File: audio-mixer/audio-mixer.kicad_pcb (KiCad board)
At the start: 2 copper layers, 72.5 x 150 mm, 49 parts, among them J1 Input A1, J10 Pot, J11 Input B3, J12 Pot, J13 Pot, J14 Output A, J15 Pot, J16 Output B, J17 AudioJack4, J18 Power, J19 Power, J2 Pot, J3 Input A2, J4 Pot, J5 Input A3, J6 Pot, J7 Input B1, J8 Pot, J9 Input B2, SW1 Mono/Stereo, U1 TL072

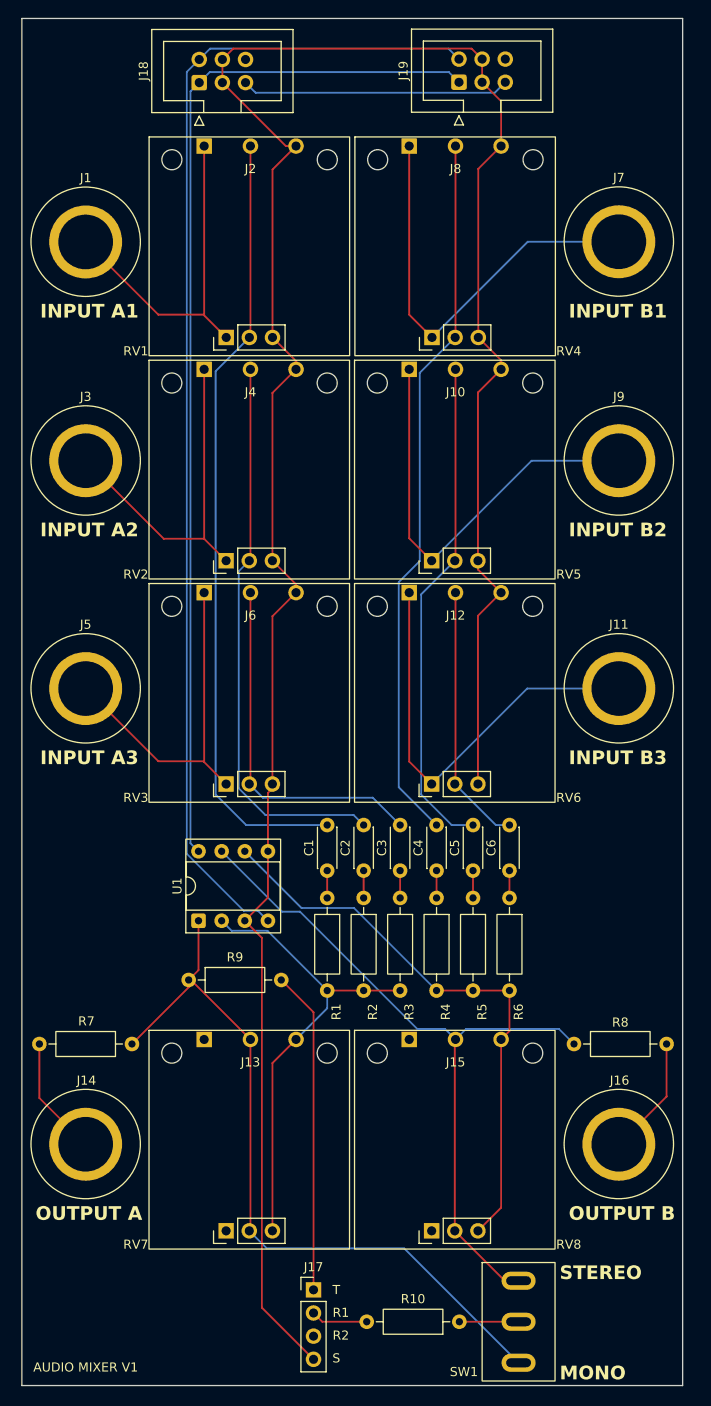
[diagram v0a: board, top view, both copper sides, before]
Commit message: More space for backup pot
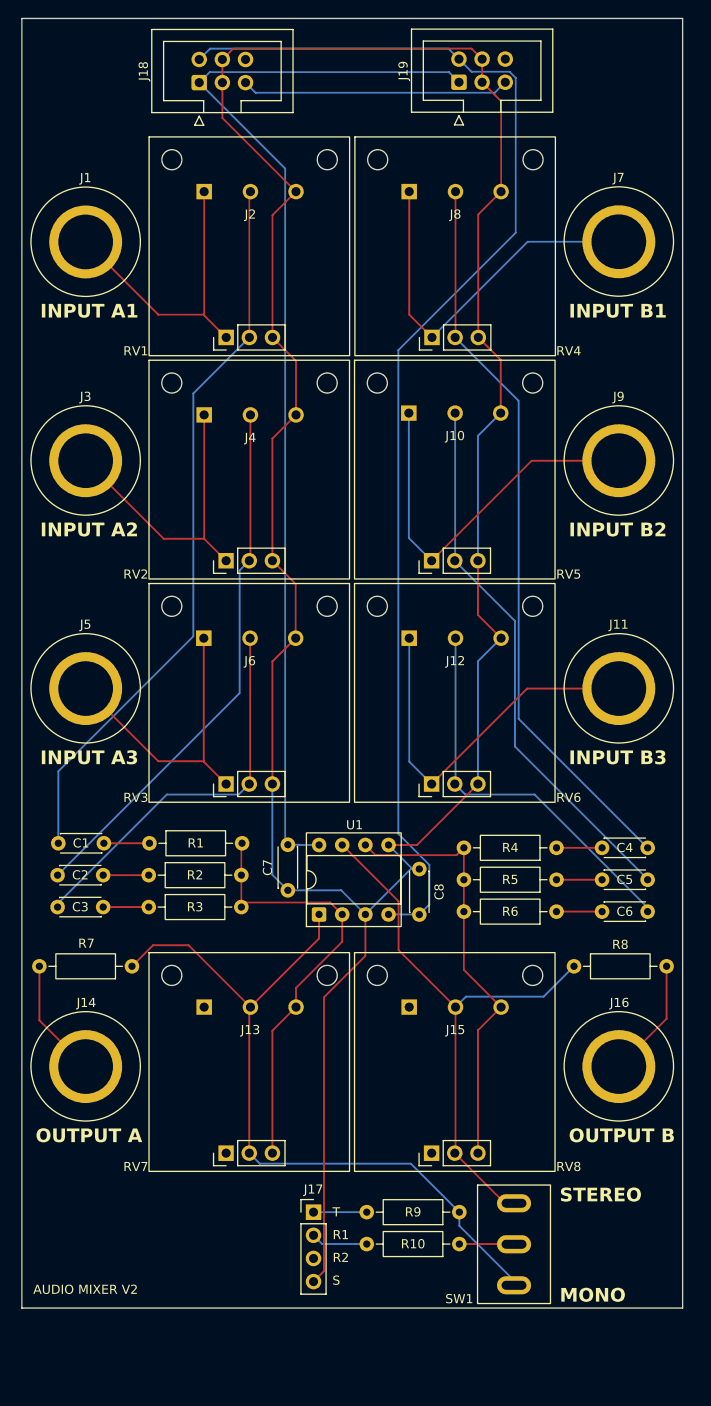
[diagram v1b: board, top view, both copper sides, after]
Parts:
- added C7: 100nF, Capacitor_THT:C_Disc_D4.3mm_W1.9mm_P5.00mm, F.Cu at (60.2, 118.2)
- added C8: 100nF, Capacitor_THT:C_Disc_D4.3mm_W1.9mm_P5.00mm, F.Cu at (74.6, 115.8)
- moved R9 39.1 mm to (79.0, 153.5), turned to 180 degrees
- moved C3 38.6 mm to (34.9, 120.0), turned to 0 degrees
- moved C2 34.0 mm to (34.9, 116.5), turned to 0 degrees
- moved C1 29.6 mm to (35.0, 113.0), turned to 0 degrees
- moved R3 27.6 mm to (44.9, 120.0), turned to 0 degrees
- moved R2 23.7 mm to (44.9, 116.5), turned to 0 degrees
- moved C4 23.3 mm to (99.7, 113.5), turned to 180 degrees
- moved R1 20.4 mm to (45.0, 113.0), turned to 0 degrees
- moved C5 20.1 mm to (99.7, 117.0), turned to 180 degrees
- moved C6 17.9 mm to (99.7, 120.5), turned to 180 degrees
- moved SW1 17.0 mm to (85.0, 157.0)
- moved R4 14.3 mm to (89.7, 113.5), turned to 180 degrees
- moved U1 13.2 mm to (63.6, 120.8)
- moved R5 9.38 mm to (89.7, 117.0), turned to 180 degrees
- moved F3 8.52 mm to (96.5, 156.5)
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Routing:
- net Net-(J17-PadT): track 35.5 -> 5.84 mm
- net GND: track 271.5 -> 292.9 mm
- net Net-(J15-Pin_2): track 78.7 -> 63.1 mm
- net Net-(J15-Pin_3): track 62.8 -> 47.8 mm
- net Net-(J12-Pin_2): track 28.9 -> 43.4 mm
- net -12V: track 129.1 -> 138.9 mm
- net Net-(J2-Pin_2): track 86.4 -> 80.2 mm
- net 12V: track 114.5 -> 120.5 mm
- net Net-(J7-Pin_1): track 46.9 -> 41.9 mm
- net Net-(J3-Pin_1): track 38.5 -> 33.5 mm
- net Net-(J11-Pin_1): track 46.9 -> 41.9 mm
- net Net-(J1-Pin_1): track 38.3 -> 33.3 mm
- net Net-(J5-Pin_1): track 38.3 -> 33.3 mm
- net Net-(J10-Pin_1): track 47.1 -> 42.3 mm
- net Net-(J10-Pin_2): track 55.3 -> 60.0 mm
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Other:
- board size 72.5 x 150 mm -> 72.5 x 141.5 mm
- board text added: "AUDIO MIXER V2"
- board text removed: "AUDIO MIXER V1"

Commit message: Various improvements
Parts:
- added G***: LOGO, modular2:ibis-small, F.Cu at (99.5, 159.0)

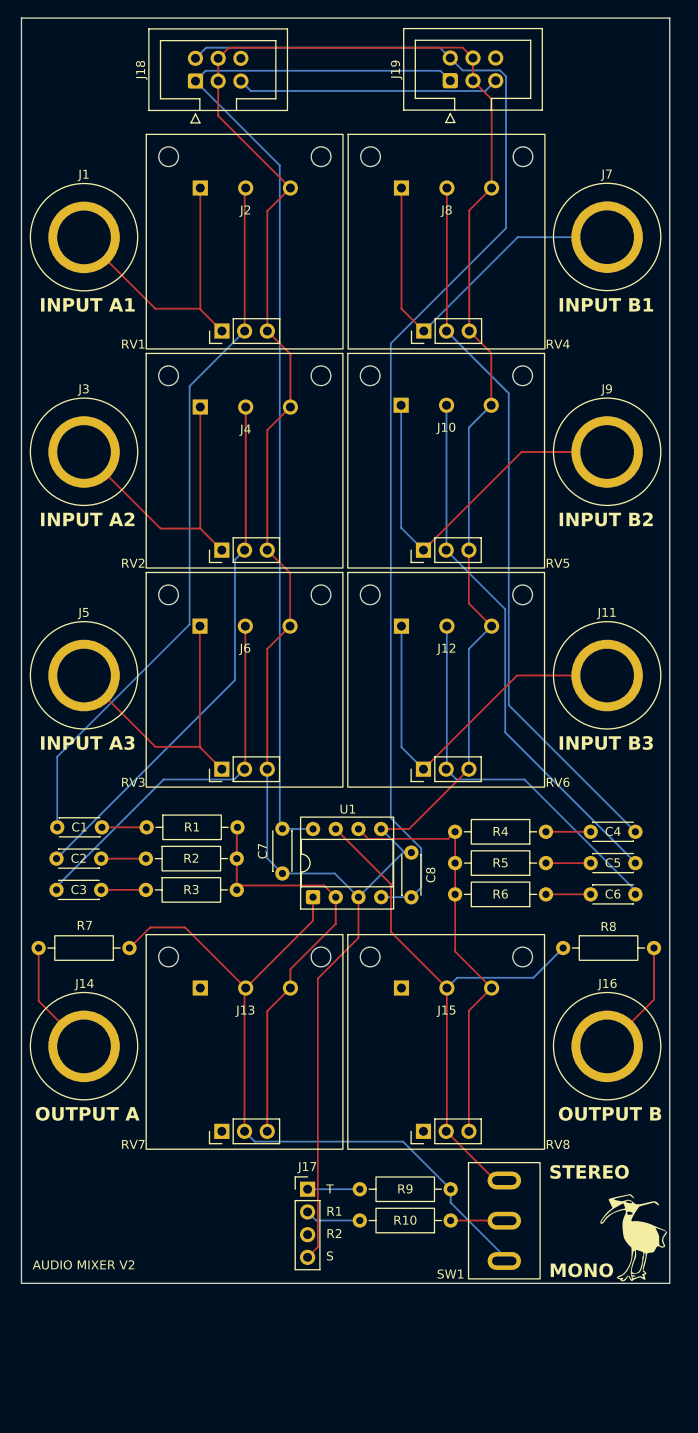
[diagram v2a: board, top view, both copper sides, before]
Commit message: Fix issues with audio mixer
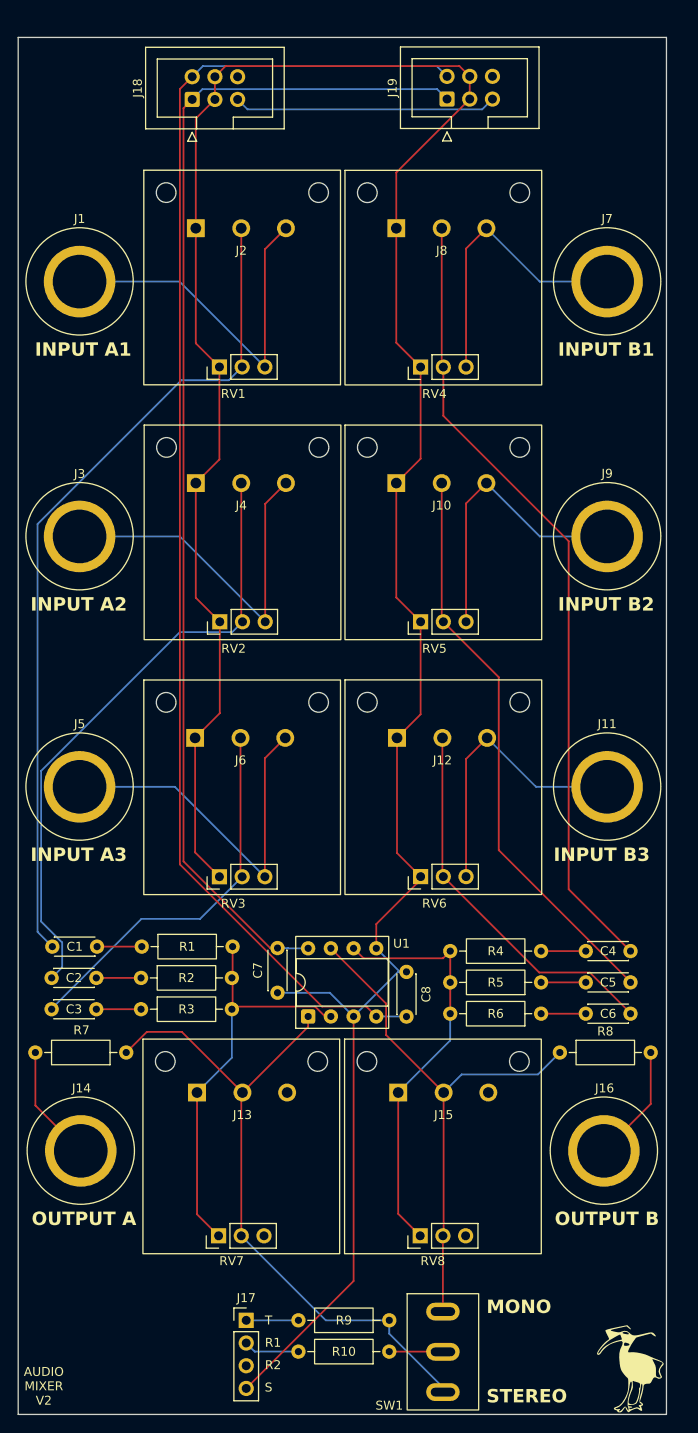
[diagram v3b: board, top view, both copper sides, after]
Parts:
- moved SW1 16.2 mm to (78.1, 171.7)
- moved J17 16.2 mm to (56.1, 168.1)
- moved R10 16.2 mm to (72.1, 171.6)
- moved R9 16.2 mm to (72.1, 168.1)
- moved G*** 14.7 mm to (99.1, 173.7)
- moved F3 14.7 mm to (96.1, 171.1)
- moved F4 14.7 mm to (37.6, 171.1)
- moved C8 13.4 mm to (74.1, 129.2)
- moved C1 13.4 mm to (34.5, 126.3)
- moved C4 13.4 mm to (99.1, 126.8)
- moved C7 13.4 mm to (59.6, 131.5)
- moved R1 13.4 mm to (44.5, 126.3)
- moved R4 13.4 mm to (89.1, 126.8)
- moved C2 13.4 mm to (34.4, 129.8)
- moved C3 13.4 mm to (34.4, 133.3)
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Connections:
- J10 pad 1: Net-(J10-Pin_1) -> GND
- J10 pad 3: GND -> Net-(J10-Pin_3)
- J12 pad 1: Net-(J11-Pin_1) -> GND
- J12 pad 3: GND -> Net-(J11-Pin_1)
- J13 pad 1: unconnected-(J13-Pin_1-Pad1) -> Net-(J13-Pin_1)
- J13 pad 3: Net-(J13-Pin_3) -> unconnected-(J13-Pin_3-Pad3)
- J15 pad 1: unconnected-(J15-Pin_1-Pad1) -> Net-(J15-Pin_1)
- J15 pad 3: Net-(J15-Pin_3) -> unconnected-(J15-Pin_3-Pad3)
- J2 pad 1: Net-(J1-Pin_1) -> GND
- J2 pad 3: GND -> Net-(J1-Pin_1)
- J4 pad 1: Net-(J3-Pin_1) -> GND
- J4 pad 3: GND -> Net-(J3-Pin_1)
- J6 pad 1: Net-(J5-Pin_1) -> GND
- J6 pad 3: GND -> Net-(J5-Pin_1)
- J8 pad 1: Net-(J7-Pin_1) -> GND
- J8 pad 3: GND -> Net-(J7-Pin_1)
- J9 pad 1: Net-(J10-Pin_1) -> Net-(J10-Pin_3)
- R1 pad 2: Net-(J13-Pin_3) -> Net-(J13-Pin_1)
- R2 pad 2: Net-(J13-Pin_3) -> Net-(J13-Pin_1)
- R3 pad 2: Net-(J13-Pin_3) -> Net-(J13-Pin_1)
- R4 pad 2: Net-(J15-Pin_3) -> Net-(J15-Pin_1)
- R5 pad 2: Net-(J15-Pin_3) -> Net-(J15-Pin_1)
- R6 pad 2: Net-(J15-Pin_3) -> Net-(J15-Pin_1)
- RV1 pad 1: Net-(J1-Pin_1) -> GND
- RV1 pad 3: GND -> Net-(J1-Pin_1)
- RV2 pad 1: Net-(J3-Pin_1) -> GND
- RV2 pad 3: GND -> Net-(J3-Pin_1)
- RV3 pad 1: Net-(J5-Pin_1) -> GND
- RV3 pad 3: GND -> Net-(J5-Pin_1)
- RV4 pad 1: Net-(J7-Pin_1) -> GND
- RV4 pad 3: GND -> Net-(J7-Pin_1)
- RV5 pad 1: Net-(J10-Pin_1) -> GND
- RV5 pad 3: GND -> Net-(J10-Pin_3)
- RV6 pad 1: Net-(J11-Pin_1) -> GND
- RV6 pad 3: GND -> Net-(J11-Pin_1)
- RV7 pad 1: unconnected-(RV7-Pad1) -> Net-(J13-Pin_1)
- RV7 pad 3: Net-(J13-Pin_3) -> unconnected-(RV7-Pad3)
- RV8 pad 1: unconnected-(RV8-Pad1) -> Net-(J15-Pin_1)
- RV8 pad 3: Net-(J15-Pin_3) -> unconnected-(RV8-Pad3)
- U1 pad 2: Net-(J13-Pin_3) -> Net-(J13-Pin_1)
- U1 pad 6: Net-(J15-Pin_3) -> Net-(J15-Pin_1)
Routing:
- net Net-(J13-Pin_3): track 48.2 -> 0.00 mm
- net Net-(J15-Pin_3): track 47.8 -> 0.00 mm
- net Net-(J15-Pin_1): track 0.00 -> 46.9 mm
- net Net-(J13-Pin_1): track 0.00 -> 46.6 mm
- net Net-(J10-Pin_1): track 42.3 -> 0.00 mm
- net Net-(J10-Pin_3): track 0.00 -> 32.4 mm
- net Net-(J2-Pin_2): track 80.2 -> 93.8 mm
- net 12V: track 120.5 -> 133.0 mm
- net -12V: track 138.9 -> 150.5 mm
- net Net-(J4-Pin_2): track 59.3 -> 69.6 mm
- net Net-(J11-Pin_1): track 41.9 -> 32.2 mm
- net GND: track 292.9 -> 302.6 mm
- net Net-(J7-Pin_1): track 41.9 -> 32.4 mm
- net Net-(J8-Pin_2): track 80.8 -> 89.6 mm
- net Net-(J5-Pin_1): track 33.3 -> 41.4 mm
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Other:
- board size 72.5 x 141.5 mm -> 72.5 x 154 mm

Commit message: Various fixes
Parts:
- added J20: Power, Connector_IDC:IDC-Header_2x03_P2.54mm_Vertical, F.Cu at (83.5, 31.5)
- moved J19 14.2 mm to (64.4, 31.6)
- moved J18 4.68 mm to (45.4, 31.5)
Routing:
- net GND: track 302.6 -> 324.8 mm
- net 5V: track 29.4 -> 40.0 mm
- net 12V: track 133.0 -> 139.2 mm
- net -12V: track 150.5 -> 152.8 mm

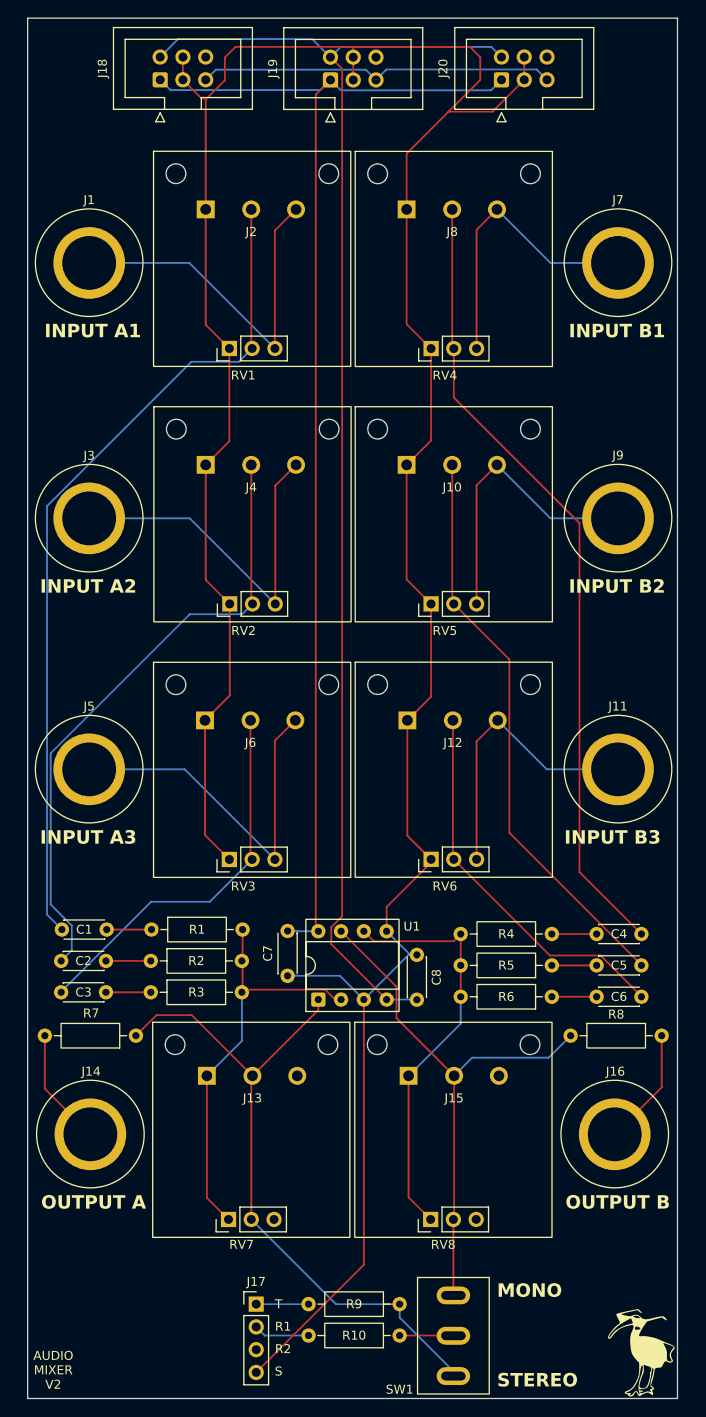
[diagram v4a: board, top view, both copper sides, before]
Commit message: Fix inverted output in audio mixer
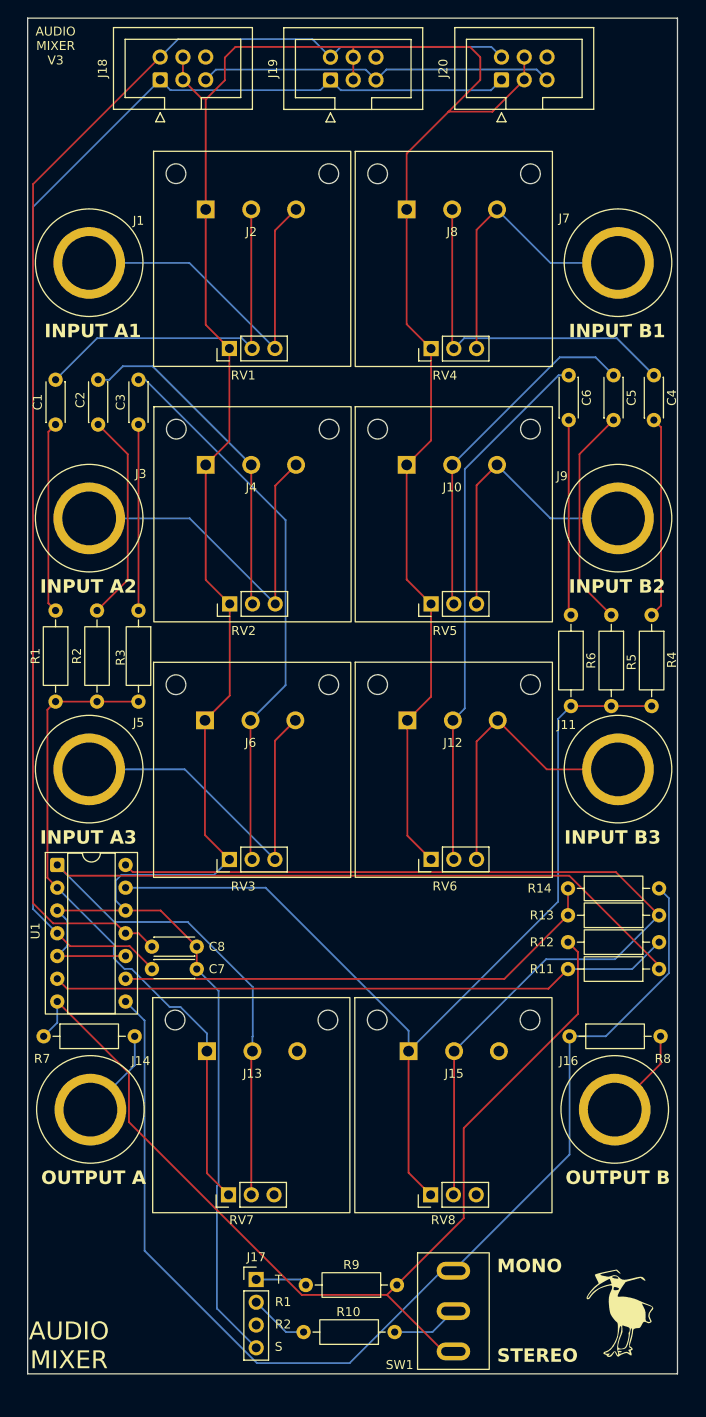
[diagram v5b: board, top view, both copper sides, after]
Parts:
- added R11: 100K, Resistor_THT:R_Axial_DIN0207_L6.3mm_D2.5mm_P10.16mm_Horizontal, F.Cu at (101.1, 130.8)
- added R12: 100K, Resistor_THT:R_Axial_DIN0207_L6.3mm_D2.5mm_P10.16mm_Horizontal, F.Cu at (101.1, 127.8)
- added R13: 100K, Resistor_THT:R_Axial_DIN0207_L6.3mm_D2.5mm_P10.16mm_Horizontal, F.Cu at (101.1, 124.8)
- added R14: 100K, Resistor_THT:R_Axial_DIN0207_L6.3mm_D2.5mm_P10.16mm_Horizontal, F.Cu at (90.9, 121.8)
- U1: value TL072 -> TL074; footprint Package_DIP:DIP-8_W7.62mm_Socket -> Package_DIP:DIP-14_W7.62mm_Socket
- moved C6 69.8 mm to (91.0, 64.5), turned to -90 degrees
- moved C3 68.9 mm to (43.0, 65.0), turned to -90 degrees
- moved C5 65.9 mm to (96.0, 64.5), turned to -90 degrees
- moved C2 65.0 mm to (38.5, 65.0), turned to -90 degrees
- moved C4 62.4 mm to (100.5, 64.5), turned to -90 degrees
- moved C1 61.3 mm to (33.8, 65.0), turned to -90 degrees
- moved R6 42.6 mm to (91.2, 91.2), turned to -90 degrees
- moved R3 42.6 mm to (43.0, 90.8), turned to -90 degrees
- moved R5 39.7 mm to (95.8, 91.2), turned to -90 degrees
- moved R2 39.5 mm to (38.4, 90.8), turned to -90 degrees
- moved R4 37.3 mm to (100.2, 91.2), turned to -90 degrees
- moved R1 37.2 mm to (33.8, 90.8), turned to -90 degrees
- moved U1 32.8 mm to (33.9, 119.1), turned to 0 degrees
- moved C8 24.6 mm to (49.5, 128.2), turned to 180 degrees
- moved R7 10.3 mm to (32.4, 138.2), turned to 0 degrees
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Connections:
- R7 pad 1: Net-(J13-Pin_2) -> Net-(SW1-C)
- R8 pad 1: Net-(J15-Pin_2) -> Net-(SW1-A)
- R9 pad 1: Net-(J13-Pin_2) -> Net-(SW1-C)
- SW1 pad 1: Net-(J13-Pin_2) -> Net-(SW1-C)
- SW1 pad 3: Net-(J15-Pin_2) -> Net-(SW1-A)
- U1 pad 4: -12V -> 12V
- U1 pad 6: Net-(J15-Pin_1) -> Net-(U1B--)
- U1 pad 7: Net-(J15-Pin_2) -> Net-(SW1-C)
- U1 pad 8: 12V -> Net-(SW1-A)
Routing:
- net Net-(SW1-A): track 0.00 -> 128.0 mm
- net Net-(SW1-C): track 0.00 -> 116.7 mm
- net Net-(U1B--): track 0.00 -> 69.7 mm
- net Net-(J15-Pin_1): track 46.9 -> 112.5 mm
- net Net-(U1C--): track 0.00 -> 55.3 mm
- net Net-(J2-Pin_2): track 93.7 -> 39.9 mm
- net Net-(J8-Pin_2): track 89.6 -> 40.1 mm
- net Net-(J13-Pin_2): track 75.5 -> 122.9 mm
- net Net-(J15-Pin_2): track 60.7 -> 107.0 mm
- net Net-(J4-Pin_2): track 69.6 -> 37.8 mm
- net Net-(J13-Pin_1): track 46.6 -> 74.2 mm
- net Net-(J10-Pin_2): track 64.6 -> 39.4 mm
- net Net-(C5-Pad2): track 5.00 -> 24.8 mm
- net Net-(J6-Pin_2): track 43.1 -> 62.5 mm
- net Net-(C2-Pad2): track 5.00 -> 23.5 mm
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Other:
- board size 72.5 x 154 mm -> 72.5 x 151.2 mm
- board text added: "AUDIO MIXER"
- board text added: "AUDIO MIXER V3"
- board text removed: "AUDIO MIXER V2"
